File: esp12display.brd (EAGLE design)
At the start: 31.5 x 30 mm, 3 parts

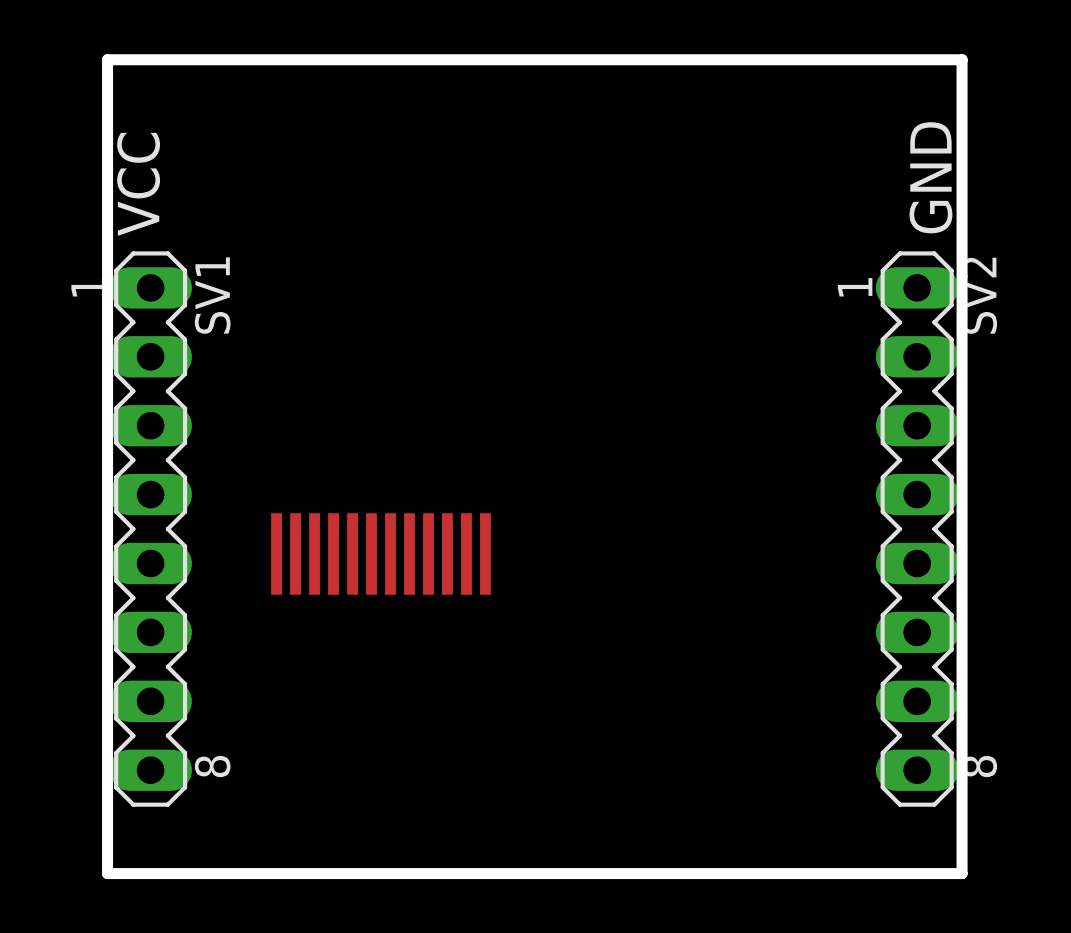
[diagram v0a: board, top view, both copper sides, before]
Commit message: some major updates
* working ft232rl layout
* replaced the DIN resistors for the WS2112 with solder jumpers
* sensors breakout board
* fixed a bug (missing trace) in the rgbwwpw board
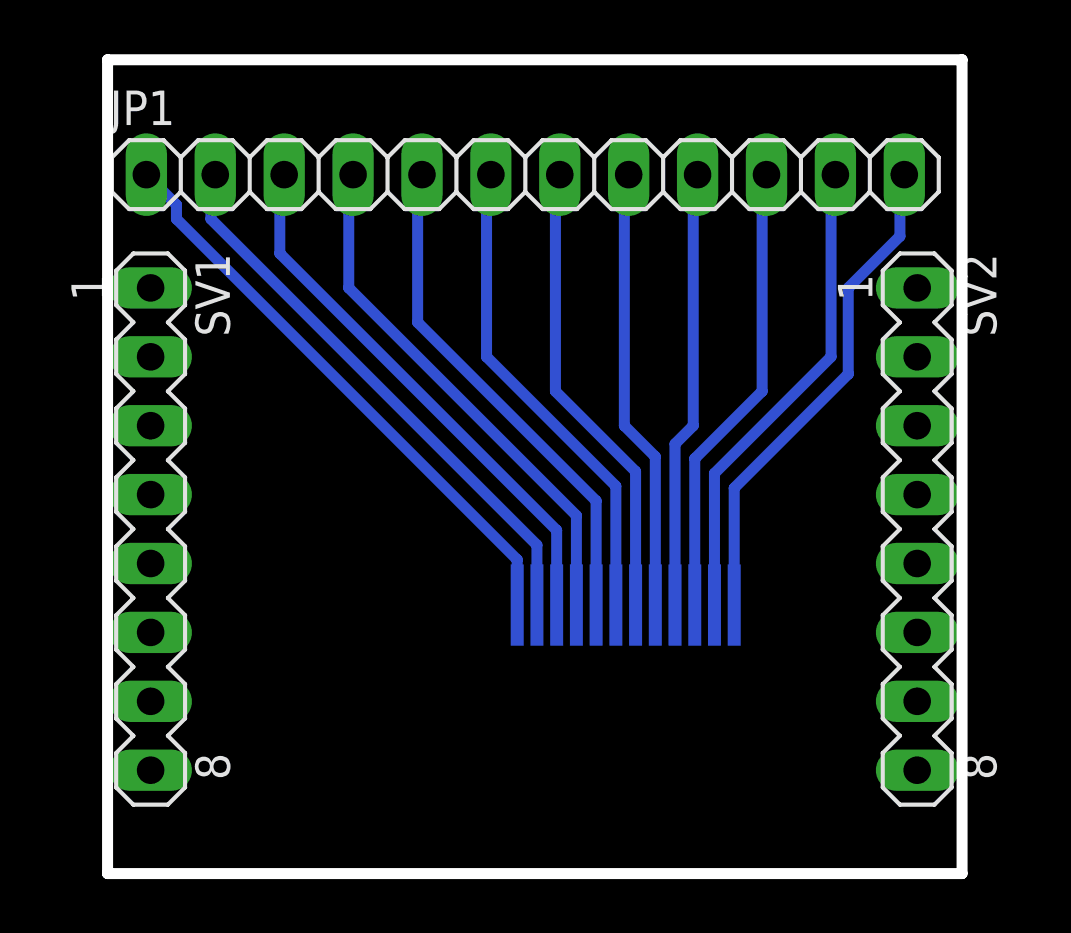
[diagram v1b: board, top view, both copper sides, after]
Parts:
- removed U$2: 12PIN_LCD_PADS, 12Pin_LCD_Connector:PINS_ONLY
- added JP1: (no value), adafruit:1X12
- added U$1: 12PIN_LCD_PADS, esp12display:PINS_ONLY
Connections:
- net N$10: now also JP1.9, U$1.4; no longer U$2.9
- net N$11: now also JP1.10, U$1.3; no longer U$2.10
- net N$12: now also JP1.11, U$1.2; no longer U$2.11
- net N$13: now also JP1.12, U$1.1; no longer U$2.12
- net N$2: now also JP1.1, U$1.12; no longer U$2.1
- net N$3: now also JP1.2, U$1.11; no longer U$2.2
- net N$4: now also JP1.3, U$1.10; no longer U$2.3
- net N$5: now also JP1.4, U$1.9; no longer U$2.4
- net N$6: now also JP1.5, U$1.8; no longer U$2.5
- net N$7: now also JP1.6, U$1.7; no longer U$2.6
- net N$8: now also JP1.7, U$1.6; no longer U$2.7
- net N$9: now also JP1.8, U$1.5; no longer U$2.8
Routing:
- net N$2: track 0.00 -> 21.5 mm
- net N$3: track 0.00 -> 20.9 mm
- net N$4: track 0.00 -> 20.2 mm
- net N$5: track 0.00 -> 19.4 mm
- net N$6: track 0.00 -> 18.7 mm
- net N$13: track 0.00 -> 18.5 mm
- net N$7: track 0.00 -> 17.9 mm
- net N$12: track 0.00 -> 17.7 mm
- net N$8: track 0.00 -> 17.2 mm
- net N$11: track 0.00 -> 17.0 mm
- net N$9: track 0.00 -> 16.4 mm
- net N$10: track 0.00 -> 16.2 mm
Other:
- board text removed: "GND"
- board text removed: "VCC"
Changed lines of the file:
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@@
 <setting verticaltext="up"/>
 </settings>
-<grid distance="50" unitdist="mil" unit="mil" style="lines" multiple="1" display="no" altdistance="25" altunitdist="mil" altunit="mil"/>
+<grid distance="0.05" unitdist="inch" unit="inch" style="lines" multiple="1" display="no" altdistance="0.025" altunitdist="inch" altunit="inch"/>
 <layers>
 <layer number="1" name="Top" color="4" fill="1" visible="yes" active="yes"/>
@@
 <wire x1="31.5" y1="30" x2="0" y2="30" width="0.4064" layer="20"/>
 <wire x1="0" y1="30" x2="0" y2="0" width="0.4064" layer="20"/>
-<text x="1.905" y="23.495" size="1.524" layer="25" rot="R90">VCC</text>
-<text x="31.115" y="23.495" size="1.524" layer="25" rot="R90">GND</text>
 <dimension x1="0" y1="0" x2="31.5" y2="0" x3="15.75" y3="-3.81" textsize="1.524" layer="16"/>
 <dimension x1="31.5" y1="0" x2="31.5" y2="30" x3="38.1" y3="15" textsize="1.524" layer="16"/>
@@
 <attribute name="MPN" value="" x="29.845" y="12.7" size="1.778" layer="27" rot="R270" display="off"/>
 </element>
-<element name="U$2" library="12Pin_LCD_Connector" package="PINS_ONLY" value="12PIN_LCD_PADS" x="11.43" y="17.78" rot="R90"/>
+<element name="U$1" library="esp12display" package="PINS_ONLY" value="12PIN_LCD_PADS" x="23.1" y="9.9" rot="MR90"/>
+<element name="JP1" library="adafruit" package="1X12" value="" x="15.4" y="25.765"/>
 </elements>
 <signals>
@@
 </signal>
 <signal name="N$2">
-<contactref element="U$2" pad="1"/>
+<contactref element="U$1" pad="12"/>
+<contactref element="JP1" pad="1"/>
+<wire x1="15.1008" y1="9.9" x2="15.1008" y2="11.5692" width="0.4064" layer="16"/>
+<wire x1="15.1008" y1="11.5692" x2="2.54" y2="24.13" width="0.4064" layer="16"/>
+<wire x1="2.54" y1="24.13" x2="2.54" y2="24.655" width="0.4064" layer="16"/>
+<wire x1="2.54" y1="24.655" x2="1.43" y2="25.765" width="0.4064" layer="16"/>
 </signal>
 <signal name="N$3">
-<contactref element="U$2" pad="2"/>
+<contactref element="U$1" pad="11"/>
+<contactref element="JP1" pad="2"/>
+<wire x1="15.828" y1="9.9" x2="15.828" y2="12.112" width="0.4064" layer="16"/>
+<wire x1="15.828" y1="12.112" x2="3.81" y2="24.13" width="0.4064" layer="16"/>
+<wire x1="3.81" y1="24.13" x2="3.81" y2="25.605" width="0.4064" layer="16"/>
+<wire x1="3.81" y1="25.605" x2="3.97" y2="25.765" width="0.4064" layer="16"/>
 </signal>
 <signal name="N$4">
-<contactref element="U$2" pad="3"/>
+<contactref element="U$1" pad="10"/>
+<contactref element="JP1" pad="3"/>
+<wire x1="16.5552" y1="9.9" x2="16.5552" y2="12.6548" width="0.4064" layer="16"/>
+<wire x1="16.5552" y1="12.6548" x2="6.35" y2="22.86" width="0.4064" layer="16"/>
+<wire x1="6.35" y1="22.86" x2="6.35" y2="25.605" width="0.4064" layer="16"/>
+<wire x1="6.35" y1="25.605" x2="6.51" y2="25.765" width="0.4064" layer="16"/>
 </signal>
 <signal name="N$5">
-<contactref element="U$2" pad="4"/>
+<contactref element="U$1" pad="9"/>
+<contactref element="JP1" pad="4"/>
+<wire x1="17.2824" y1="9.9" x2="17.2824" y2="13.1976" width="0.4064" layer="16"/>
+<wire x1="17.2824" y1="13.1976" x2="8.89" y2="21.59" width="0.4064" layer="16"/>
+<wire x1="8.89" y1="21.59" x2="8.89" y2="25.605" width="0.4064" layer="16"/>
+<wire x1="8.89" y1="25.605" x2="9.05" y2="25.765" width="0.4064" layer="16"/>
 </signal>
 <signal name="N$6">
-<contactref element="U$2" pad="5"/>
+<contactref element="U$1" pad="8"/>
+<contactref element="JP1" pad="5"/>
+<wire x1="18.0096" y1="9.9" x2="18.0096" y2="13.7404" width="0.4064" layer="16"/>
+<wire x1="18.0096" y1="13.7404" x2="11.43" y2="20.32" width="0.4064" layer="16"/>
+<wire x1="11.43" y1="20.32" x2="11.43" y2="25.605" width="0.4064" layer="16"/>
+<wire x1="11.43" y1="25.605" x2="11.59" y2="25.765" width="0.4064" layer="16"/>
 </signal>
 <signal name="N$7">
-<contactref element="U$2" pad="6"/>
+<contactref element="U$1" pad="7"/>
+<contactref element="JP1" pad="6"/>
+<wire x1="18.7368" y1="9.9" x2="18.7368" y2="14.2832" width="0.4064" layer="16"/>
+<wire x1="18.7368" y1="14.2832" x2="13.97" y2="19.05" width="0.4064" layer="16"/>
+<wire x1="13.97" y1="19.05" x2="13.97" y2="25.605" width="0.4064" layer="16"/>
+<wire x1="13.97" y1="25.605" x2="14.13" y2="25.765" width="0.4064" layer="16"/>
 </signal>
 <signal name="N$8">
-<contactref element="U$2" pad="7"/>
+<contactref element="U$1" pad="6"/>
+<contactref element="JP1" pad="7"/>
+<wire x1="19.464" y1="9.9" x2="19.464" y2="14.826" width="0.4064" layer="16"/>
+<wire x1="19.464" y1="14.826" x2="16.51" y2="17.78" width="0.4064" layer="16"/>
+<wire x1="16.51" y1="17.78" x2="16.51" y2="25.605" width="0.4064" layer="16"/>
+<wire x1="16.51" y1="25.605" x2="16.67" y2="25.765" width="0.4064" layer="16"/>
 </signal>
 <signal name="N$9">
-<contactref element="U$2" pad="8"/>
+<contactref element="U$1" pad="5"/>
+<contactref element="JP1" pad="8"/>
+<wire x1="20.1912" y1="9.9" x2="20.1912" y2="15.3688" width="0.4064" layer="16"/>
+<wire x1="20.1912" y1="15.3688" x2="19.05" y2="16.51" width="0.4064" layer="16"/>
+<wire x1="19.05" y1="16.51" x2="19.05" y2="25.605" width="0.4064" layer="16"/>
+<wire x1="19.05" y1="25.605" x2="19.21" y2="25.765" width="0.4064" layer="16"/>
 </signal>
 <signal name="N$10">
-<contactref element="U$2" pad="9"/>
+<contactref element="U$1" pad="4"/>
+<contactref element="JP1" pad="9"/>
+<wire x1="20.9184" y1="9.9" x2="20.9184" y2="15.8384" width="0.4064" layer="16"/>
+<wire x1="20.9184" y1="15.8384" x2="21.59" y2="16.51" width="0.4064" layer="16"/>
+<wire x1="21.59" y1="16.51" x2="21.59" y2="25.605" width="0.4064" layer="16"/>
+<wire x1="21.59" y1="25.605" x2="21.75" y2="25.765" width="0.4064" layer="16"/>
 </signal>
 <signal name="N$11">
-<contactref element="U$2" pad="10"/>
+<contactref element="U$1" pad="3"/>
+<contactref element="JP1" pad="10"/>
+<wire x1="21.6456" y1="9.9" x2="21.6456" y2="15.2956" width="0.4064" layer="16"/>
+<wire x1="21.6456" y1="15.2956" x2="24.13" y2="17.78" width="0.4064" layer="16"/>
+<wire x1="24.13" y1="17.78" x2="24.13" y2="25.605" width="0.4064" layer="16"/>
+<wire x1="24.13" y1="25.605" x2="24.29" y2="25.765" width="0.4064" layer="16"/>
 </signal>
 <signal name="N$12">
-<contactref element="U$2" pad="11"/>
+<contactref element="U$1" pad="2"/>
+<contactref element="JP1" pad="11"/>
+<wire x1="22.3728" y1="9.9" x2="22.3728" y2="14.7528" width="0.4064" layer="16"/>
+<wire x1="22.3728" y1="14.7528" x2="26.67" y2="19.05" width="0.4064" layer="16"/>
+<wire x1="26.67" y1="19.05" x2="26.67" y2="25.605" width="0.4064" layer="16"/>
+<wire x1="26.67" y1="25.605" x2="26.83" y2="25.765" width="0.4064" layer="16"/>
 </signal>
 <signal name="N$13">
-<contactref element="U$2" pad="12"/>
+<contactref element="U$1" pad="1"/>
+<contactref element="JP1" pad="12"/>
+<wire x1="23.1" y1="9.9" x2="23.1" y2="14.21" width="0.4064" layer="16"/>
+<wire x1="23.1" y1="14.21" x2="27.305" y2="18.415" width="0.4064" layer="16"/>
+<wire x1="27.305" y1="18.415" x2="27.305" y2="21.59" width="0.4064" layer="16"/>
+<wire x1="27.305" y1="21.59" x2="29.21" y2="23.495" width="0.4064" layer="16"/>
+<wire x1="29.21" y1="23.495" x2="29.21" y2="25.605" width="0.4064" layer="16"/>
+<wire x1="29.21" y1="25.605" x2="29.37" y2="25.765" width="0.4064" layer="16"/>
 </signal>
 </signals>
